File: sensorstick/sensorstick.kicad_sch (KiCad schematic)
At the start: 5 parts, among them U1 ESP32-C3_SUPERMINI

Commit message: fix pins
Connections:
- net +3.3V: now also OLED1.2 (VCC); no longer USB1.1 (VCC)
- net +5V: now also USB1.1 (VCC); no longer OLED1.2 (VCC)

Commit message: progress
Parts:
- BT1: now not fitted; now left out of the parts list
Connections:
- net i2c_scl: now reaches U1.0 (GPIO0)
- net i2c_scl: now also OLED1.3 (SCL), U2.3 (SCL)
- net i2c_sda: now reaches U1.1 (GPIO1)
- net i2c_sda: now also OLED1.4 (SDA), U2.4 (SDA)
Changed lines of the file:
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@@
+	(wire
+		(pts
+			(xy 142.24 46.99) (xy 154.94 46.99)
+		)
+		(stroke
+			(width 0)
+			(type default)
+		)
+	)
 	(wire
 		(pts
@@
 			(width 0)
 			(type default)
+		)
+	)
+	(wire
+		(pts
+			(xy 154.94 49.53) (xy 142.24 49.53)
+		)
+		(stroke
+			(width 0)
+			(type default)
+		)
+	)
+	(global_label "i2c_sda"
+		(shape input)
+		(at 154.94 49.53 0)
+		(fields_autoplaced yes)
+		(effects
+			(font
+				(size 1.27 1.27)
+			)
+			(justify left)
+		)
+		(property "Intersheetrefs" "${INTERSHEET_REFS}"
+			(at 165.1218 49.53 0)
+			(effects
+				(font
+					(size 1.27 1.27)
+				)
+				(justify left)
+				(hide yes)
+			)
+		)
+	)
+	(global_label "i2c_sda"
+		(shape output)
+		(at 45.72 50.8 180)
+		(fields_autoplaced yes)
+		(effects
+			(font
+				(size 1.27 1.27)
+			)
+			(justify right)
+		)
+		(property "Intersheetrefs" "${INTERSHEET_REFS}"
+			(at 35.5382 50.8 0)
+			(effects
+				(font
+					(size 1.27 1.27)
+				)
+				(justify right)
+				(hide yes)
+			)
+		)
+	)
+	(global_label "i2c_scl"
+		(shape output)
+		(at 45.72 48.26 180)
+		(fields_autoplaced yes)
+		(effects
+			(font
+				(size 1.27 1.27)
+			)
+			(justify right)
+		)
+		(property "Intersheetrefs" "${INTERSHEET_REFS}"
+			(at 36.0824 48.26 0)
+			(effects
+				(font
+					(size 1.27 1.27)
+				)
+				(justify right)
+				(hide yes)
+			)
+		)
+	)
+	(global_label "i2c_sda"
+		(shape input)
+		(at 123.19 69.85 0)
+		(fields_autoplaced yes)
+		(effects
+			(font
+				(size 1.27 1.27)
+			)
+			(justify left)
+		)
+		(property "Intersheetrefs" "${INTERSHEET_REFS}"
+			(at 133.3718 69.85 0)
+			(effects
+				(font
+					(size 1.27 1.27)
+				)
+				(justify left)
+				(hide yes)
+			)
+		)
+	)
+	(global_label "i2c_scl"
+		(shape input)
+		(at 123.19 72.39 0)
+		(fields_autoplaced yes)
+		(effects
+			(font
+				(size 1.27 1.27)
+			)
+			(justify left)
+		)
+		(property "Intersheetrefs" "${INTERSHEET_REFS}"
+			(at 132.8276 72.39 0)
+			(effects
+				(font
+					(size 1.27 1.27)
+				)
+				(justify left)
+				(hide yes)
+			)
+		)
+	)
+	(global_label "i2c_scl"
+		(shape input)
+		(at 154.94 46.99 0)
+		(fields_autoplaced yes)
+		(effects
+			(font
+				(size 1.27 1.27)
+			)
+			(justify left)
+		)
+		(property "Intersheetrefs" "${INTERSHEET_REFS}"
+			(at 164.5776 46.99 0)
+			(effects
+				(font
+					(size 1.27 1.27)
+				)
+				(justify left)
+				(hide yes)
+			)
 		)
 	)
@@
 		(at 27.94 34.29 0)
 		(unit 1)
-		(exclude_from_sim no)
-		(in_bom yes)
-		(on_board yes)
-		(dnp no)
+		(exclude_from_sim yes)
+		(in_bom no)
+		(on_board no)
+		(dnp yes)
 		(fields_autoplaced yes)
 		(property "Reference" "BT1"

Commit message: update
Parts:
- OLED1: LCSC Part C5248081 -> (none)
- U1: Availability Not in stock -> (none); Check_prices https://www.snapeda.com/parts/ESP32-C3%20SuperMini_TH/Espre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 -> (none); Description_1 Super tiny ESP32-C3 board -> (none); MANUFACTURER Espressif -> (none); MAXIMUM_PACKAGE_HEIGHT 4.2mm -> (none); MF Espressif Systems -> (none); MP ESP32-C3 SuperMini_TH -> (none); Package Package -> (none); Price None -> (none); STANDARD Manufacturer Recommendations -> (none); SnapEDA_Link https://www.snapeda.com/parts/ESP32-C3%20SuperMini_TH/Espre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 -> (none)
- USB1: LCSC Part C319178 -> (none)
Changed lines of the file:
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@@
 		(dnp no)
 		(fields_autoplaced yes)
-		(property "Reference" "#PWR01"
+		(property "Reference" "#PWR1"
 			(at 77.47 40.64 0)
 			(effects
@@
 			(project ""
 				(path "/7be59ae3-cff4-4640-882e-dfffcfbe988a"
-					(reference "#PWR01")
+					(reference "#PWR1")
 					(unit 1)
 				)
@@
 		(on_board yes)
 		(dnp no)
-		(property "Reference" "#PWR05"
+		(property "Reference" "#PWR5"
 			(at 25.4 55.88 0)
 			(effects
@@
 			(project ""
 				(path "/7be59ae3-cff4-4640-882e-dfffcfbe988a"
-					(reference "#PWR05")
+					(reference "#PWR5")
 					(unit 1)
 				)
@@
 		(dnp no)
 		(fields_autoplaced yes)
-		(property "Reference" "#PWR07"
+		(property "Reference" "#PWR7"
 			(at 77.47 43.18 0)
 			(effects
@@
 			(project ""
 				(path "/7be59ae3-cff4-4640-882e-dfffcfbe988a"
-					(reference "#PWR07")
+					(reference "#PWR7")
 					(unit 1)
 				)
@@
 		(dnp no)
 		(fields_autoplaced yes)
-		(property "Reference" "#PWR011"
+		(property "Reference" "#PWR11"
 			(at 27.94 43.18 0)
 			(effects
@@
 			(project ""
 				(path "/7be59ae3-cff4-4640-882e-dfffcfbe988a"
-					(reference "#PWR011")
+					(reference "#PWR11")
 					(unit 1)
 				)
@@
 		(dnp no)
 		(fields_autoplaced yes)
-		(property "Reference" "#PWR06"
+		(property "Reference" "#PWR6"
 			(at 33.02 66.04 0)
 			(effects
@@
 			(project ""
 				(path "/7be59ae3-cff4-4640-882e-dfffcfbe988a"
-					(reference "#PWR06")
+					(reference "#PWR6")
 					(unit 1)
 				)
@@
 			)
 		)
-		(property "MF" "Espressif Systems"
-			(at 63.5 53.34 0)
-			(effects
-				(font
-					(size 1.27 1.27)
-				)
-				(justify bottom)
-				(hide yes)
-			)
-		)
-		(property "MAXIMUM_PACKAGE_HEIGHT" "4.2mm"
-			(at 63.5 53.34 0)
-			(effects
-				(font
-					(size 1.27 1.27)
-				)
-				(justify bottom)
-				(hide yes)
-			)
-		)
-		(property "Package" "Package"
-			(at 63.5 53.34 0)
-			(effects
-				(font
-					(size 1.27 1.27)
-				)
-				(justify bottom)
-				(hide yes)
-			)
-		)
-		(property "Price" "None"
-			(at 63.5 53.34 0)
-			(effects
-				(font
-					(size 1.27 1.27)
-				)
-				(justify bottom)
-				(hide yes)
-			)
-		)
-		(property "Check_prices" "https://www.snapeda.com/parts/ESP32-C3%20SuperMini_TH/Espressif+Systems/view-part/?ref=eda"
-			(at 63.5 53.34 0)
-			(effects
-				(font
-					(size 1.27 1.27)
-				)
-				(justify bottom)
-				(hide yes)
-			)
-		)
-		(property "STANDARD" "Manufacturer Recommendations"
-			(at 63.5 53.34 0)
-			(effects
-				(font
-					(size 1.27 1.27)
-				)
-				(justify bottom)
-				(hide yes)
-			)
-		)
-		(property "PARTREV" ""
-			(at 63.5 53.34 0)
-			(effects
-				(font
-					(size 1.27 1.27)
-				)
-				(justify bottom)
-				(hide yes)
-			)
-		)
-		(property "SnapEDA_Link" "https://www.snapeda.com/parts/ESP32-C3%20SuperMini_TH/Espressif+Systems/view-part/?ref=snap"
-			(at 63.5 53.34 0)
-			(effects
-				(font
-					(size 1.27 1.27)
-				)
-				(justify bottom)
-				(hide yes)
-			)
-		)
-		(property "MP" "ESP32-C3 SuperMini_TH"
-			(at 63.5 53.34 0)
-			(effects
-				(font
-					(size 1.27 1.27)
-				)
-				(justify bottom)
-				(hide yes)
-			)
-		)
-		(property "Description_1" "\nSuper tiny ESP32-C3 board\n"
-			(at 63.5 53.34 0)
-			(effects
-				(font
-					(size 1.27 1.27)
-				)
-				(justify bottom)
-				(hide yes)
-			)
-		)
-		(property "Availability" "Not in stock"
-			(at 63.5 53.34 0)
-			(effects
-				(font
-					(size 1.27 1.27)
-				)
-				(justify bottom)
-				(hide yes)
-			)
-		)
-		(property "MANUFACTURER" "Espressif"
-			(at 63.5 53.34 0)
-			(effects
-				(font
-					(size 1.27 1.27)
-				)
-				(justify bottom)
-				(hide yes)
-			)
-		)
 		(pin "21"
 		)
@@
 		(dnp no)
 		(fields_autoplaced yes)
-		(property "Reference" "#PWR03"
+		(property "Reference" "#PWR3"
 			(at 129.54 77.47 0)
 			(effects
@@
 			(project ""
 				(path "/7be59ae3-cff4-4640-882e-dfffcfbe988a"
-					(reference "#PWR03")
+					(reference "#PWR3")
 					(unit 1)
 				)
@@
 		(dnp no)
 		(fields_autoplaced yes)
-		(property "Reference" "#PWR02"
+		(property "Reference" "#PWR2"
 			(at 87.63 68.58 0)
 			(effects
@@
 			(project ""
 				(path "/7be59ae3-cff4-4640-882e-dfffcfbe988a"
-					(reference "#PWR02")
+					(reference "#PWR2")
 					(unit 1)
 				)
@@
 		(dnp no)
 		(fields_autoplaced yes)
-		(property "Reference" "#PWR04"
+		(property "Reference" "#PWR4"
 			(at 119.38 74.93 0)
 			(effects
@@
 			(project ""
 				(path "/7be59ae3-cff4-4640-882e-dfffcfbe988a"
-					(reference "#PWR04")
+					(reference "#PWR4")
 					(unit 1)
 				)
@@
 		(dnp no)
 		(fields_autoplaced yes)
-		(property "Reference" "#PWR08"
+		(property "Reference" "#PWR8"
 			(at 157.48 36.83 0)
 			(effects
@@
 			(project ""
 				(path "/7be59ae3-cff4-4640-882e-dfffcfbe988a"
-					(reference "#PWR08")
+					(reference "#PWR8")
 					(unit 1)
 				)
@@
 			)
 		)
-		(property "LCSC Part" "C319178"
-			(at 27.94 85.09 0)
-			(effects
-				(font
-					(size 1.27 1.27)
-				)
-				(hide yes)
-			)
-		)
 		(pin "5"
 		)
@@
 		(dnp no)
 		(fields_autoplaced yes)
-		(property "Reference" "#PWR010"
+		(property "Reference" "#PWR10"
 			(at 27.94 33.02 0)
 			(effects
@@
 			(project ""
 				(path "/7be59ae3-cff4-4640-882e-dfffcfbe988a"
-					(reference "#PWR010")
+					(reference "#PWR10")
 					(unit 1)
 				)
@@
 		(dnp no)
 		(fields_autoplaced yes)
-		(property "Reference" "#PWR09"
+		(property "Reference" "#PWR9"
 			(at 158.75 44.45 0)
 			(effects
@@
 			(project ""
 				(path "/7be59ae3-cff4-4640-882e-dfffcfbe988a"
-					(reference "#PWR09")
+					(reference "#PWR9")
 					(unit 1)
 				)
@@
 			(effects
 				(font
-					(size 1.27 1.27)
-				)
-				(hide yes)
-			)
-		)
-		(property "LCSC Part" "C5248081"
-			(at 118.11 87.63 0)
-			(effects
-				(font

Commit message: add condensator
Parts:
- added C1, C2, C3: C, Capacitor_SMD:C_0603_1608Metric, symbol Device:C
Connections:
- net +3.3V: now also C1.1, C2.1
- net +5V: now also C3.1
- net GND: now also C1.2, C2.2, C3.2

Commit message: update
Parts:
- removed BT1: Battery_Cell, CustomLibrary:BatteryHolder_Keystone_1060_1x2032, symbol Device:Battery_Cell
- OLED1: LCSC Part (none) -> C5248081
- U1: Availability (none) -> Not in stock; Check_prices (none) -> https://www.snapeda.com/parts/ESP32-C3%20SuperMini_TH/Espre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; Description_1 (none) -> Super tiny ESP32-C3 board; MANUFACTURER (none) -> Espressif; MAXIMUM_PACKAGE_HEIGHT (none) -> 4.2mm; MF (none) -> Espressif Systems; MP (none) -> ESP32-C3 SuperMini_TH; Package (none) -> Package; Price (none) -> None; STANDARD (none) -> Manufacturer Recommendations; SnapEDA_Link (none) -> https://www.snapeda.com/parts/ESP32-C3%20SuperMini_TH/Espre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
- USB1: LCSC Part (none) -> C319178
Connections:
- net GND: now also USB1.5, USB1.6
- no-connect marks 0 -> 14

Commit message: set LCSC #
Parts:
- C1, C2, C3: value C -> 100nF
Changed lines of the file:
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@@
 			)
 		)
-		(property "Value" "C"
+		(property "Value" "100nF"
 			(at 154.94 41.9099 0)
 			(effects
@@
 			)
 		)
-		(property "Value" "C"
+		(property "Value" "100nF"
 			(at 135.89 78.74 90)
 			(effects
@@
 			)
 		)
-		(property "Value" "C"
+		(property "Value" "100nF"
 			(at 90.17 55.8799 0)
 			(effects

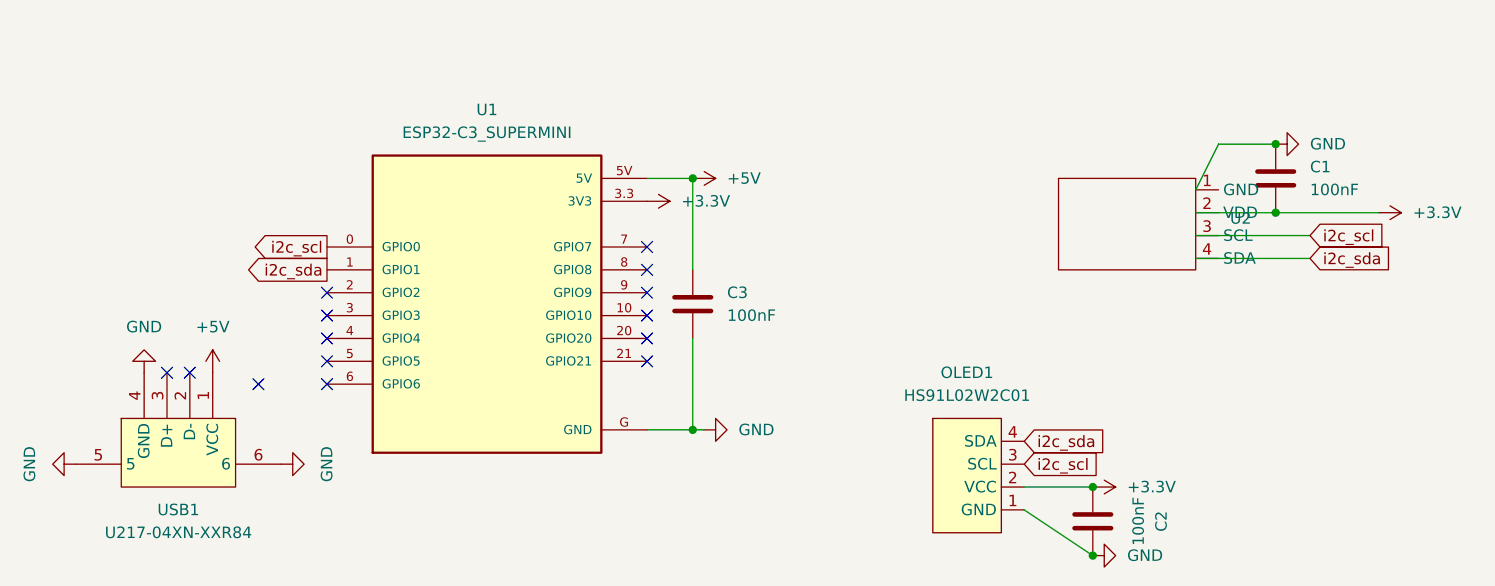
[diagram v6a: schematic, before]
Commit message: update filter
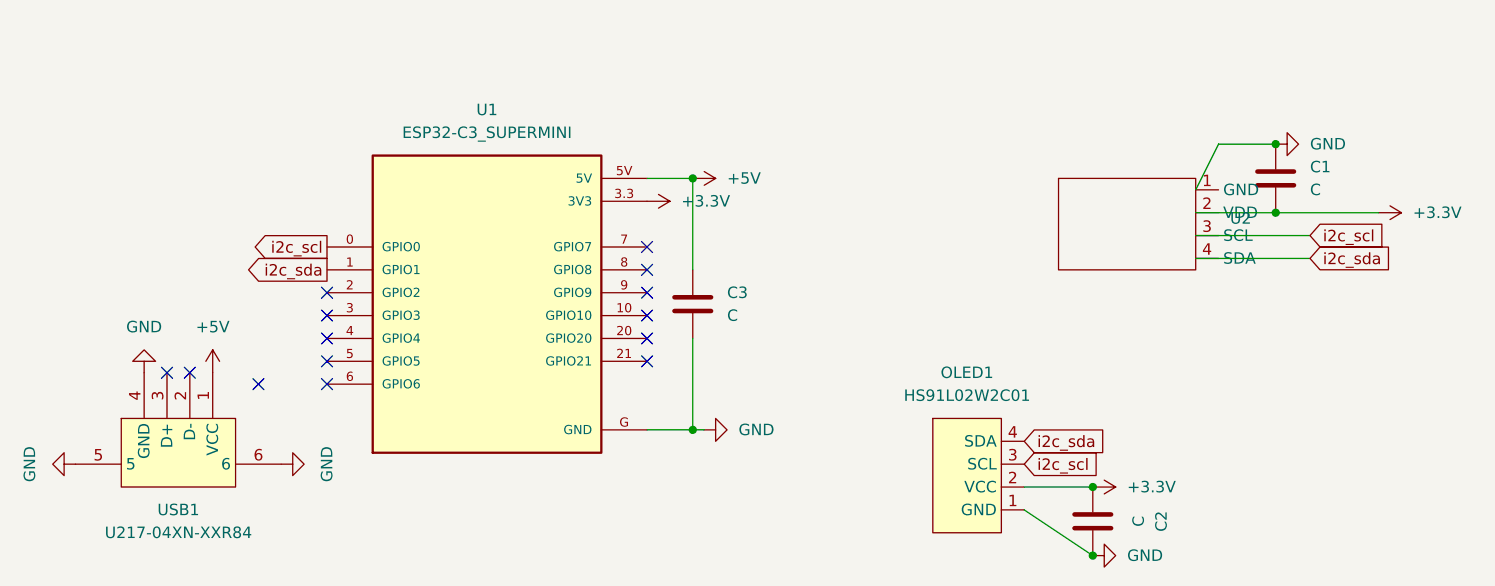
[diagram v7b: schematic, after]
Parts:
- C1, C2, C3: value 100nF -> C
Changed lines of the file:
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@@
 			)
 		)
-		(property "Value" "100nF"
+		(property "Value" "C"
 			(at 154.94 41.9099 0)
 			(effects
@@
 		(on_board yes)
 		(dnp no)
-		(property "Reference" "#PWR010"
+		(property "Reference" "#PWR10"
 			(at 46.99 72.39 0)
 			(effects
@@
 			(project "sensorstick"
 				(path "/7be59ae3-cff4-4640-882e-dfffcfbe988a"
-					(reference "#PWR010")
+					(reference "#PWR10")
 					(unit 1)
 				)
@@
 			)
 		)
-		(property "Value" "100nF"
+		(property "Value" "C"
 			(at 135.89 78.74 90)
 			(effects
@@
 			)
 		)
-		(property "Value" "100nF"
+		(property "Value" "C"
 			(at 90.17 55.8799 0)
 			(effects
@@
 		(on_board yes)
 		(dnp no)
-		(property "Reference" "#PWR011"
+		(property "Reference" "#PWR11"
 			(at 11.43 72.39 0)
 			(effects
@@
 			(project "sensorstick"
 				(path "/7be59ae3-cff4-4640-882e-dfffcfbe988a"
-					(reference "#PWR011")
-					(unit 1)
-				)
+					(reference "#PWR11")
+					(unit 1)
+				)

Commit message: set value
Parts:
- C1, C2, C3: value C -> 100nF
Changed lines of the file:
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@@
 			)
 		)
-		(property "Value" "C"
+		(property "Value" "100nF"
 			(at 154.94 41.9099 0)
 			(effects
@@
 			)
 		)
-		(property "Value" "C"
+		(property "Value" "100nF"
 			(at 135.89 78.74 90)
 			(effects
@@
 			)
 		)
-		(property "Value" "C"
+		(property "Value" "100nF"
 			(at 90.17 55.8799 0)
 			(effects
